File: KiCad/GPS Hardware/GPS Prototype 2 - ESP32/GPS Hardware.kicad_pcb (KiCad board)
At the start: 4 copper layers, 200 x 70 mm, 69 parts, among them J1 USB_C_Receptacle_USB2.0, J2 Conn_01x04_Male, J3 Conn_Coaxial, J4 Conn_01x13_Male, J5 B2B-XH-A(LF)(SN), J6 SIM8065-6-1-14-01-A_REVA1, Q1 BC847, Q2 BC847, Q3 BSS84, U1 ESP32-WROOM-32D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

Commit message: Alvin house Mo update
Have your kicad update
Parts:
- U10: moved to B.Cu
- moved U3 337.4 mm to (60.5, 68.6), turned to 270 degrees
- moved J5 333.5 mm to (53.3, 78.3), turned to 90 degrees
- moved J1 326.2 mm to (60.0, 53.8), turned to 180 degrees
- moved U4 319.7 mm to (97.3, 72.6), turned to 270 degrees
- moved J3 290.2 mm to (53.2, 112.9)
- moved J6 278.5 mm to (69.2, 139.2)
- moved U8 255.3 mm to (70.0, 116.2), turned to 90 degrees
- moved U10 254.6 mm to (100.8, 96.4)
- moved S2 244.7 mm to (122.1, 99.5), turned to 90 degrees
- moved J2 237.8 mm to (139.4, 101.2), turned to 90 degrees
- moved S1 213.3 mm to (143.3, 65.1), turned to 270 degrees
- moved U1 197.9 mm to (139.8, 86.4), turned to 270 degrees
- moved J4 191.5 mm to (146.9, 109.9), turned to 270 degrees
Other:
- board size 200 x 70 mm -> 100 x 100 mm

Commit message: Push to laptop
Add traces etc.
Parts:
- C23: moved to B.Cu
- moved R12 325.4 mm to (54.3, 133.4), turned to 90 degrees
- moved R13 313.1 mm to (64.8, 101.2), turned to 270 degrees
- moved C2 307.6 mm to (122.2, 134.3), turned to 180 degrees
- moved R8 300.4 mm to (135.6, 136.9), turned to 180 degrees
- moved C9 297.6 mm to (121.4, 120.4), turned to 90 degrees
- moved L1 293.2 mm to (130.6, 124.6)
- moved R10 292.6 mm to (122.2, 126.6), turned to 180 degrees
- moved R1 291.2 mm to (141.9, 141.7), turned to 180 degrees
- moved C17 290.4 mm to (90.3, 104.4), turned to 90 degrees
- moved C1 289.4 mm to (127.9, 134.3), turned to 180 degrees
- moved R7 288.2 mm to (138.3, 129.3), turned to 180 degrees
- moved TH1 286.6 mm to (140.7, 116.5)
- moved C4 286.5 mm to (122.2, 130.3), turned to 180 degrees
- moved R6 285.1 mm to (138.3, 133.0)
- moved U7 285.1 mm to (92.7, 123.7)
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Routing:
- net D+: track 0.00 -> 17.7 mm
- net D-: track 0.00 -> 17.7 mm

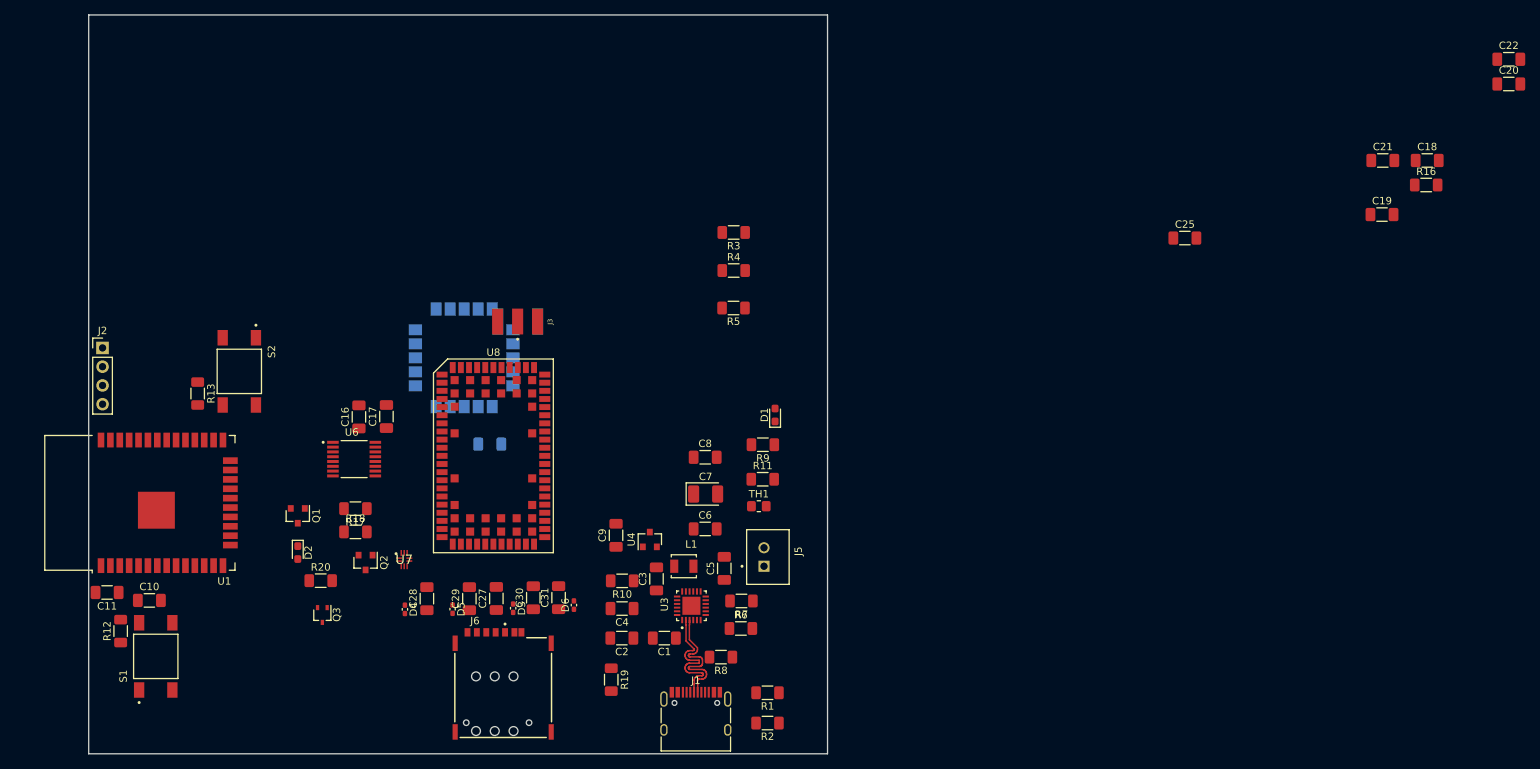
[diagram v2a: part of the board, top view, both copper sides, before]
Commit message: Update to Uni computers
Finish esp32 connections.
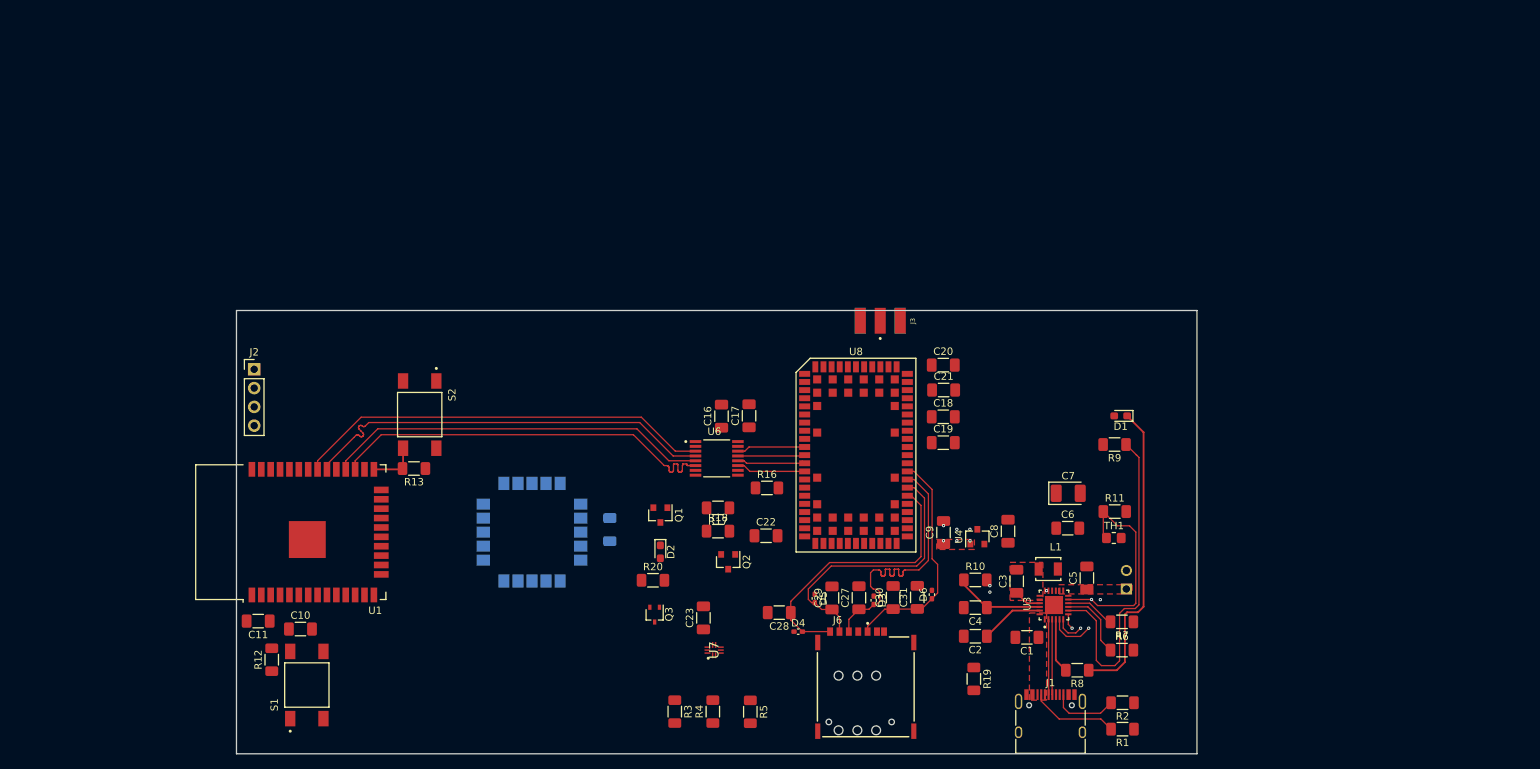
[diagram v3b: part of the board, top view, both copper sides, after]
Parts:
- C23: moved to F.Cu
- C25, J5: moved to B.Cu
- moved C22 119.4 mm to (141.7, 120.5)
- moved R16 98.2 mm to (141.8, 114.0)
- moved C25 87.3 mm to (120.5, 119.7), turned to 270 degrees
- moved C20 85.5 mm to (165.7, 97.4)
- moved C18 74.1 mm to (165.7, 104.4)
- moved C21 67.1 mm to (165.7, 100.8)
- moved C19 66.9 mm to (165.7, 107.9)
- moved R3 65.3 mm to (129.3, 144.3), turned to 270 degrees
- moved R4 59.8 mm to (134.5, 144.3), turned to 90 degrees
- moved R5 54.7 mm to (139.6, 144.3), turned to 270 degrees
- moved D4 53.3 mm to (146.0, 133.5), turned to 0 degrees
- moved R6 51.7 mm to (189.8, 136.0)
- moved R7 51.6 mm to (189.8, 132.1)
- moved L1 49.3 mm to (179.9, 125.0)
- moved C5 49.1 mm to (185.1, 126.2)
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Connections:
- U1 pad 27: RX -> TX
- U1 pad 28: TX -> RX
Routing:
- net RTS: track 0.00 -> 56.7 mm
- net CTS: track 0.00 -> 56.7 mm
- net TX: track 0.00 -> 54.1 mm
- net RX: track 0.00 -> 52.1 mm
- net Net-(R9-Pad1): track 0.00 -> 45.5 mm
- net Net-(R10-Pad2): track 0.00 -> 43.2 mm, vias 0 -> 2
- net Net-(D1-Pad1): track 0.00 -> 41.5 mm
- net CLK: track 0.00 -> 38.7 mm
- net RST: track 0.00 -> 37.5 mm
- net IO: track 0.00 -> 37.1 mm
- net VSIM: track 0.00 -> 30.8 mm
- net Net-(C4-Pad1): track 0.00 -> 12.3 mm
- net Net-(J1-PadA5): track 0.00 -> 11.9 mm
- net Net-(R6-Pad1): track 0.00 -> 9.78 mm
- net TX_Cellular: track 0.00 -> 9.64 mm
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- added copper zone on F.Cu, net +3V3
- added copper zone on F.Cu, net Net-(C3-Pad2)
- added copper zone on F.Cu, net Net-(C5-Pad1)
- added copper zone on F.Cu, net VBUS
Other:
- board size 100 x 100 mm -> 130 x 60 mm

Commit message: Update from Uni
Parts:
- moved R5 30.4 mm to (109.1, 144.6)
- moved R3 30.4 mm to (98.9, 144.6)
- moved R4 30.4 mm to (104.0, 144.6)
- moved U7 23.3 mm to (120.4, 117.5)
- moved C22 22.7 mm to (120.6, 112.0), turned to 90 degrees
- moved Q1 20.9 mm to (133.9, 137.6)
- moved D2 19.6 mm to (133.9, 141.1)
- moved Q3 13.0 mm to (125.8, 118.2), turned to 180 degrees
- moved C23 12.0 mm to (124.8, 123.0), turned to 270 degrees
- moved R20 9.47 mm to (130.5, 118.0), turned to 270 degrees
- moved Q2 3.97 mm to (132.6, 124.3), turned to 180 degrees
- moved R18 1.25 mm to (136.4, 120.0)
- moved R17 1.25 mm to (136.4, 116.8)
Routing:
- net GPIO4: track 0.00 -> 72.9 mm
- net GPIO3: track 0.00 -> 71.2 mm
- net PWR_Cellular: track 0.00 -> 51.1 mm
- net RESET_Cellular: track 0.00 -> 45.2 mm
- net +1V8: track 0.00 -> 38.5 mm
- net GPIO2: track 0.00 -> 17.9 mm
- net Net-(R17-Pad1): track 0.00 -> 9.66 mm
- net Net-(Q2-Pad3): track 0.00 -> 9.11 mm
- net VCC_GPS: track 0.00 -> 4.48 mm, vias 0 -> 1
- net Net-(Q1-Pad1): track 0.00 -> 3.58 mm
- net GND: vias 6 -> 7

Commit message: Update
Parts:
- moved J4 138.6 mm to (118.3, 145.7), turned to 270 degrees
- moved R4 46.8 mm to (78.4, 105.4), turned to 270 degrees
- moved R3 46.0 mm to (74.6, 105.5), turned to 90 degrees
- moved R5 32.0 mm to (78.4, 135.5)
- moved R12 8.94 mm to (74.2, 146.2), turned to 180 degrees
- moved C10 6.10 mm to (73.0, 135.3), turned to 180 degrees
- moved J2 4.07 mm to (74.2, 94.3), turned to 90 degrees
- moved S1 2.40 mm to (77.3, 141.6), turned to 180 degrees
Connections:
- J4 pad 1: /MCU Schematic/IO2 -> /MCU Schematic/IO4
- J4 pad 10: /MCU Schematic/IO33 -> /MCU Schematic/IO32
- J4 pad 12: /MCU Schematic/SENS_VP -> /MCU Schematic/SENS_VN
- J4 pad 13: /MCU Schematic/SENS_VN -> /MCU Schematic/SENS_VP
- J4 pad 2: /MCU Schematic/IO4 -> /MCU Schematic/IO5
- J4 pad 3: /MCU Schematic/IO5 -> /MCU Schematic/IO2
- J4 pad 4: /MCU Schematic/IO12 -> /MCU Schematic/IO15
- J4 pad 6: /MCU Schematic/IO14 -> /MCU Schematic/IO12
- J4 pad 7: /MCU Schematic/IO15 -> /MCU Schematic/IO14
- J4 pad 9: /MCU Schematic/IO32 -> /MCU Schematic/IO33
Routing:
- net PWR_Cellular: track 51.1 -> 105.3 mm, vias 0 -> 4
- net /MCU Schematic/IO5: track 0.00 -> 52.4 mm
- net /MCU Schematic/IO4: track 0.00 -> 49.5 mm
- net /MCU Schematic/IO2: track 0.00 -> 41.9 mm
- net /MCU Schematic/IO15: track 0.00 -> 39.5 mm
- net /MCU Schematic/IO13: track 0.00 -> 29.6 mm
- net /MCU Schematic/SENS_VN: track 0.00 -> 26.1 mm
- net /MCU Schematic/IO33: track 0.00 -> 25.9 mm
- net /MCU Schematic/IO32: track 0.00 -> 25.3 mm
- net /MCU Schematic/SENS_VP: track 0.00 -> 25.3 mm
- net /MCU Schematic/IO35: track 0.00 -> 25.1 mm
- net /MCU Schematic/IO12: track 0.00 -> 24.2 mm
- net /MCU Schematic/IO14: track 0.00 -> 23.7 mm
- net /MCU Schematic/IO27: track 0.00 -> 23.2 mm
- net Net-(C10-Pad1): track 0.00 -> 7.98 mm
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
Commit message: Update to Laptop
Still a lot more to go
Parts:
- removed U4: LM3480-3.3, Package_TO_SOT_SMD:SOT-23
- added C12: 100u, Capacitor_Tantalum_SMD:CP_EIA-6032-15_Kemet-U_Pad2.25x2.35mm_HandSolder, F.Cu at (241.9, 112.0)
- added C13: 4u7, Capacitor_SMD:C_1206_3216Metric_Pad1.33x1.80mm_HandSolder, B.Cu at (110.3, 109.6)
- added C14: 4u7, Capacitor_SMD:C_1206_3216Metric_Pad1.33x1.80mm_HandSolder, B.Cu at (110.3, 106.2)
- added D7: SP712-02HTG, GPS Hardware:SOT95P237X115-3N, F.Cu at (188.8, 134.0)
- added J7: Conn_01x08_Male, Connector_PinHeader_2.54mm:PinHeader_1x08_P2.54mm_Vertical_SMD_Pin1Left, F.Cu at (94.4, 139.8)
- added U2: MIC5209-4.2YS-TR, Package_TO_SOT_SMD:SOT-223, F.Cu at (155.8, 141.0)
- C27, C28, C29, C30, C31, D3, D4, D5, D6, J6: moved to B.Cu
- C8: value 0u1 -> 10u
- J2: footprint Connector_PinHeader_2.54mm:PinHeader_1x04_P2.54mm_Vertical -> Connector_PinHeader_2.54mm:PinHeader_1x04_P2.54mm_Vertical_SMD_Pin1Left
- J4: value Conn_01x13_Male -> Conn_01x05_Male; footprint Connector_PinHeader_2.54mm:PinHeader_1x13_P2.54mm_Vertical -> Connector_PinHeader_2.54mm:PinHeader_1x05_P2.54mm_Vertical_SMD_Pin1Left
- moved C8 66.1 mm to (240.4, 116.0), turned to 0 degrees
- moved C9 64.7 mm to (230.3, 116.2), turned to 0 degrees
- moved D1 40.7 mm to (154.8, 125.3), turned to 270 degrees
- moved J6 40.1 mm to (184.8, 113.9), turned to 270 degrees
- moved R8 36.9 mm to (215.2, 158.1), turned to 270 degrees
- moved R9 35.1 mm to (158.7, 126.2), turned to 270 degrees
- moved J4 33.1 mm to (97.0, 120.3), turned to 0 degrees
- moved C7 24.7 mm to (165.3, 132.4), turned to 90 degrees
- moved R11 22.9 mm to (167.8, 126.1), turned to 90 degrees
- moved R1 22.8 mm to (197.2, 125.1), turned to 270 degrees
- moved C30 20.8 mm to (175.1, 115.8), turned to 180 degrees
- moved J1 19.9 mm to (196.6, 134.8), turned to 90 degrees
- moved R10 19.8 mm to (177.0, 145.0), turned to 90 degrees
- moved R2 18.4 mm to (193.6, 125.1), turned to 270 degrees
- moved C4 18.3 mm to (180.8, 145.0), turned to 270 degrees
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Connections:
- C9 pad 1: +3V3 -> SYS
- J2 pad 2: TX_MCU -> RX_MCU
- J2 pad 3: RX_MCU -> TX_MCU
- U1 pad 10: PWR_Cellular -> RESET_Cellular
- U1 pad 37: RESET_Cellular -> PWR_Cellular
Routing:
- net GPIO4: track 72.9 -> 0.55 mm
- net GPIO3: track 71.2 -> 0.00 mm
- net RESET_Cellular: track 45.2 -> 0.00 mm
- net Net-(D1-Pad1): track 41.5 -> 0.00 mm
- net /MCU Schematic/IO4: track 49.5 -> 10.3 mm
- net CLK: track 38.7 -> 0.00 mm
- net RST: track 37.5 -> 0.00 mm
- net IO: track 37.1 -> 0.00 mm
- net /MCU Schematic/IO5: track 52.4 -> 19.4 mm
- net /MCU Schematic/IO2: track 41.9 -> 9.95 mm
- net VSIM: track 30.8 -> 0.00 mm
- net SDA_Power: track 4.07 -> 31.3 mm, vias 1 -> 2
- net /MCU Schematic/IO15: track 39.5 -> 14.6 mm
- net /MCU Schematic/IO13: track 29.6 -> 6.19 mm
- net GPIO2: track 20.1 -> 0.02 mm
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- removed copper zone on F.Cu, net +3V3

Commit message: Update to laptop
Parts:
- removed D3, D4, D5, D6: PESD0402, Capacitor_SMD:C_0402_1005Metric_Pad0.74x0.62mm_HandSolder
- R11, TH1: moved to B.Cu
- moved C12 103.1 mm to (142.8, 140.5), turned to 270 degrees
- moved C8 95.6 mm to (154.6, 158.2)
- moved C9 95.6 mm to (144.5, 158.4)
- moved C28 38.6 mm to (173.0, 106.0)
- moved C29 29.9 mm to (172.9, 109.0), turned to 180 degrees
- moved C27 25.3 mm to (172.9, 111.8), turned to 180 degrees
- moved R2 20.2 mm to (190.8, 145.0), turned to 90 degrees
- moved R1 20.0 mm to (195.4, 145.0), turned to 90 degrees
- moved R11 18.4 mm to (185.8, 129.9), turned to 270 degrees
- moved J5 13.1 mm to (176.9, 128.1), turned to 0 degrees
- moved TH1 11.6 mm to (182.5, 129.3), turned to 270 degrees
- moved R6 4.32 mm to (190.8, 125.5)
- moved R7 3.69 mm to (186.3, 125.5)
- moved C31 2.42 mm to (172.9, 118.0)
- moved C30 2.31 mm to (172.9, 115.1)
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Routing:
- net Net-(R9-Pad1): track 45.5 -> 0.00 mm
- net Net-(R10-Pad2): track 28.7 -> 0.00 mm, vias 2 -> 0
- net Net-(C4-Pad1): track 12.3 -> 0.16 mm
- net Net-(J1-PadA5): track 11.9 -> 0.00 mm
- net Net-(R6-Pad1): track 9.78 -> 0.00 mm
- net Net-(J1-PadB5): track 9.11 -> 0.00 mm
- net Net-(C2-Pad1): track 8.59 -> 0.00 mm
- net Net-(R7-Pad2): track 6.76 -> 0.00 mm
- net SDA_Power: vias 2 -> 1
- net SCL_Power: vias 2 -> 1
- net GND: vias 7 -> 4

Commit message: update to pc
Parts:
- moved C31 22.2 mm to (194.4, 112.6), turned to 270 degrees
- moved C30 18.8 mm to (191.5, 112.6), turned to 270 degrees
- moved C27 15.6 mm to (188.4, 112.5), turned to 270 degrees
- moved J6 14.1 mm to (189.8, 100.7), turned to 0 degrees
- moved C29 13.0 mm to (185.5, 112.5), turned to 270 degrees
- moved C28 11.5 mm to (182.4, 112.5), turned to 270 degrees
- moved C3 0.72 mm to (177.2, 138.7)
- moved R2 0.55 mm to (190.8, 144.5)
- moved R1 0.52 mm to (195.3, 144.5)
- moved C5 0.43 mm to (177.0, 130.0)
- moved J5 0.43 mm to (177.3, 128.0)
- moved R9 0.30 mm to (158.5, 125.9)
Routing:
- net Net-(C3-Pad1): track 3.69 -> 2.97 mm
